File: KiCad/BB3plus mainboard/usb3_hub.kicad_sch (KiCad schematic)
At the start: 73 parts, among them IC16 USB5807C/KD, IC17 TPS62933ODRLR, Y2 VXM7-9032-25M0000000

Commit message: #23
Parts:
- R62, R63: now fitted; now in the parts list
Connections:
- net HUB_VBUS_EN: no longer names the net of IC16.24 (VBUS_DET), R62.2, R63.2
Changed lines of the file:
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@@
 	(title_block
 		(title "${project_name}")
-		(date "2026-10-08")
+		(date "2026-10-09")
 		(rev "${project_version}")
 		(company "${project_creator}")
@@
 	)
 	(junction
-		(at 58.42 22.86)
-		(diameter 0)
-		(color 0 0 0 0)
-	)
-	(junction
 		(at 43.18 55.88)
 		(diameter 0)
@@
 		)
 	)
-	(wire
-		(pts
-			(xy 48.26 17.78) (xy 58.42 17.78)
-		)
-		(stroke
-			(width 0)
-			(type default)
-		)
-	)
 	(polyline
 		(pts
@@
 		)
 	)
-	(wire
-		(pts
-			(xy 58.42 17.78) (xy 58.42 22.86)
-		)
-		(stroke
-			(width 0)
-			(type default)
-		)
-	)
 	(polyline
 		(pts
@@
 		)
 	)
-	(global_label "HUB_VBUS_EN"
-		(shape input)
-		(at 48.26 17.78 180)
-		(fields_autoplaced yes)
-		(effects
-			(font
-				(size 0.889 0.889)
-				(color 204 102 0 1)
-			)
-			(justify right)
-		)
-		(property "Intersheetrefs" "${INTERSHEET_REFS}"
-			(at 37.3576 17.78 0)
-			(hide yes)
-			(show_name no)
-			(do_not_autoplace no)
-			(effects
-				(font
-					(size 1.27 1.27)
-				)
-				(justify right)
-			)
-		)
-	)
 	(global_label "DIB4_USB_RX+"
 		(shape input)
@@
 		(body_style 1)
 		(exclude_from_sim no)
-		(in_bom no)
+		(in_bom yes)
 		(on_board yes)
-		(in_pos_files no)
-		(dnp yes)
+		(in_pos_files yes)
+		(dnp no)
 		(property "Reference" "R62"
 			(at 50.8 21.59 90)
@@
 		(body_style 1)
 		(exclude_from_sim no)
-		(in_bom no)
+		(in_bom yes)
 		(on_board yes)
-		(in_pos_files no)
-		(dnp yes)
+		(in_pos_files yes)
+		(dnp no)
 		(property "Reference" "R63"
 			(at 50.8 29.21 90)

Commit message: PE fault detection section updated
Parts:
- renumbered C99 to C100, C100 to C101, C101 to C102, C102 to C103, C103 to C104, C104 to C105, C105 to C106, C106 to C107, C107 to C108, C108 to C109, C109 to C110, C110 to C111, C67 to C68, C68 to C69, C69 to C70, C70 to C71, C71 to C72, C72 to C73, C73 to C74, C74 to C75, C75 to C76, C76 to C77, C77 to C78, C78 to C79, C79 to C80, C80 to C81, C81 to C82, C82 to C83, C83 to C84, C84 to C85, C85 to C86, C86 to C87, C87 to C88, C88 to C89, C89 to C90, C90 to C91, C91 to C92, C92 to C93, C93 to C94, C94 to C95, C95 to C96, C96 to C97, C97 to C98, C98 to C99, JP10 to JP12, JP11 to JP13, JP12 to JP14, JP13 to JP15

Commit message: #24
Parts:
- renumbered C102 to C100, C103 to C101, C104 to C102, C105 to C103, C106 to C104, C107 to C105, C108 to C106, C109 to C107, C110 to C108, C111 to C109, C68 to C66, C69 to C67, C70 to C68, C71 to C69, C72 to C70, C73 to C71, C74 to C72, C75 to C73, C76 to C74, C77 to C75, C78 to C76, C79 to C77, C80 to C78, C81 to C79, C82 to C80, C83 to C81, C84 to C82, C85 to C83, C86 to C84, C87 to C85, C88 to C86, C89 to C87, C90 to C88, C91 to C89, C92 to C90, C93 to C91, C94 to C92, C95 to C93, C96 to C94, C97 to C95, C98 to C96, C99 to C97, C100 to C98, C101 to C99, IC16 to IC13, IC17 to IC14, JP12 to JP11, JP13 to JP12, JP14 to JP13, JP15 to JP14, R60 to R57, R61 to R58, R62 to R59, R63 to R60, R64 to R61, R65 to R62, R66 to R63, R67 to R64, R68 to R65, R69 to R66, R70 to R67, R71 to R68, R72 to R69, R73 to R70, R74 to R71, R75 to R72, R76 to R73, R77 to R74

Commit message: USB CC wiring updated
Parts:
- R63: value 200K -> 10K; DigiKey 13-RC0603FR-13200KLCT-ND -> 1712-CRGH0603F10KCT-ND; LCSC C25811 -> C25804; Mouser 603-RC0603FR-13200KL -> 756-WCR0603-10KFI; TME SMD0603-200K-1% -> SMD0603-10K-1%
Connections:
- net +3V3: no longer R63.1
- net GND: now also R63.1
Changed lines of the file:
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@@
 	(title_block
 		(title "${project_name}")
-		(date "2026-10-12")
+		(date "2026-10-14")
 		(rev "${project_version}")
 		(company "${project_creator}")
@@
 		)
 	)
-	(text_box "Battery charging enabled on P1 "
+	(text_box "Battery charging enabled on P1, P2"
 		(exclude_from_sim no)
-		(at 20.955 54.61 0)
-		(size 12.7 3.81)
+		(at 19.05 57.785 0)
+		(size 14.605 4.195)
 		(margins 0.6668 0.6668 0.6668 0.6668)
 		(stroke
@@
 	)
 	(junction
-		(at 43.18 55.88)
+		(at 43.18 58.42)
 		(diameter 0)
 		(color 0 0 0 0)
@@
 		)
 	)
+	(wire
+		(pts
+			(xy 43.18 58.42) (xy 43.18 60.96)
+		)
+		(stroke
+			(width 0)
+			(type default)
+		)
+	)
 	(polyline
 		(pts
@@
 	(wire
 		(pts
-			(xy 33.02 60.96) (xy 45.72 60.96)
-		)
-		(stroke
-			(width 0)
-			(type default)
-		)
-	)
-	(wire
-		(pts
 			(xy 53.34 142.24) (xy 58.42 142.24)
 		)
@@
 	(wire
 		(pts
+			(xy 43.18 60.96) (xy 45.72 60.96)
+		)
+		(stroke
+			(width 0)
+			(type default)
+		)
+	)
+	(wire
+		(pts
 			(xy 40.64 147.32) (xy 40.64 152.4)
 		)
@@
 	(wire
 		(pts
+			(xy 43.18 58.42) (xy 43.18 55.88)
+		)
+		(stroke
+			(width 0)
+			(type default)
+		)
+	)
+	(wire
+		(pts
 			(xy 271.78 147.32) (xy 274.32 147.32)
 		)
@@
 	(wire
 		(pts
-			(xy 43.18 55.88) (xy 43.18 58.42)
-		)
-		(stroke
-			(width 0)
-			(type default)
-		)
-	)
-	(wire
-		(pts
 			(xy 116.84 167.64) (xy 134.62 167.64)
 		)
@@
 	(wire
 		(pts
-			(xy 40.64 55.88) (xy 43.18 55.88)
+			(xy 40.64 58.42) (xy 43.18 58.42)
 		)
 		(stroke
@@
 		(in_pos_files yes)
 		(dnp no)
-		(property "Reference" "#+3V029"
+		(property "Reference" "#+3V028"
 			(at 279.4 30.48 0)
 			(hide yes)
@@
 			(project "BB3plus mainboard"
 				(path "/1df84e4f-233a-4f72-9418-c0020706bb76/99b67fa5-56ce-4798-a21a-d86c3d347c55"
-					(reference "#+3V029")
-					(unit 1)
-				)
-			)
-		)
-	)
-	(symbol
-		(lib_id "PCM_EEZ_symbols:+3V3")
-		(at 30.48 60.96 90)
-		(mirror x)
-		(unit 1)
-		(body_style 1)
-		(exclude_from_sim no)
-		(in_bom yes)
-		(on_board yes)
-		(in_pos_files yes)
-		(dnp no)
-		(property "Reference" "#+3V027"
-			(at 30.48 60.96 0)
-			(hide yes)
-			(show_name no)
-			(do_not_autoplace no)
-			(effects
-				(font
-					(size 1.27 1.27)
-				)
-			)
-		)
-		(property "Value" "+3V3"
-			(at 24.765 61.595 90)
-			(show_name no)
-			(do_not_autoplace no)
-			(effects
-				(font
-					(size 1.27 1.27)
-				)
-				(justify right bottom)
-			)
-		)
-		(property "Footprint" ""
-			(at 30.48 60.96 0)
-			(hide yes)
-			(show_name no)
-			(do_not_autoplace no)
-			(effects
-				(font
-					(size 1.27 1.27)
-				)
-			)
-		)
-		(property "Datasheet" ""
-			(at 30.48 60.96 0)
-			(hide yes)
-			(show_name no)
-			(do_not_autoplace no)
-			(effects
-				(font
-					(size 1.27 1.27)
-				)
-			)
-		)
-		(property "Description" ""
-			(at 30.48 60.96 0)
-			(hide yes)
-			(show_name no)
-			(do_not_autoplace no)
-			(effects
-				(font
-					(size 1.27 1.27)
-				)
-			)
-		)
-		(pin "1"
-		)
-		(instances
-			(project "BB3plus mainboard"
-				(path "/1df84e4f-233a-4f72-9418-c0020706bb76/99b67fa5-56ce-4798-a21a-d86c3d347c55"
-					(reference "#+3V027")
+					(reference "#+3V028")
 					(unit 1)
 				)
@@
 	(symbol
 		(lib_id "power:GND")
-		(at 40.64 55.88 0)
+		(at 40.64 58.42 0)
 		(mirror y)
 		(unit 1)
@@
 		(dnp no)
 		(property "Reference" "#PWR021"
-			(at 40.64 62.23 0)
+			(at 40.64 64.77 0)
 			(hide yes)
 			(show_name no)
@@
 		)
 		(property "Value" "GND"
-			(at 39.37 57.785 0)
+			(at 39.37 60.325 0)
 			(show_name no)
 			(do_not_autoplace no)
@@
 		)
 		(property "Footprint" ""
-			(at 40.64 55.88 0)
+			(at 40.64 58.42 0)
 			(hide yes)
 			(show_name no)
@@
 		)
 		(property "Datasheet" ""
-			(at 40.64 55.88 0)
+			(at 40.64 58.42 0)
 			(hide yes)
 			(show_name no)
@@
 		)
 		(property "Description" "Power symbol creates a global label with name \"GND\" , ground"
-			(at 40.64 55.88 0)
+			(at 40.64 58.42 0)
 			(hide yes)
 			(show_name no)
@@
 			)
 		)
-		(property "Value" "200K"
+		(property "Value" "10K"
 			(at 53.975 60.96 90)
 			(show_name no)
@@
 			)
 		)
-		(property "DigiKey" "13-RC0603FR-13200KLCT-ND"
+		(property "DigiKey" "1712-CRGH0603F10KCT-ND"
 			(at 50.8 60.96 0)
 			(hide yes)
@@
 			)
 		)
-		(property "Mouser" "603-RC0603FR-13200KL "
+		(property "Mouser" "756-WCR0603-10KFI"
 			(at 50.8 60.96 0)
 			(hide yes)
@@
 			)
 		)
-		(property "TME" "SMD0603-200K-1%"
+		(property "TME" "SMD0603-10K-1%"
 			(at 50.8 60.96 0)
 			(hide yes)
@@
 			)
 		)
-		(property "LCSC" "C25811"
+		(property "LCSC" "C25804"
 			(at 50.8 60.96 0)
 			(hide yes)
@@
 		(in_pos_files yes)
 		(dnp no)
-		(property "Reference" "#+3V028"
+		(property "Reference" "#+3V027"
 			(at 38.1 71.12 0)
 			(hide yes)
@@
 			(project "BB3plus mainboard"
 				(path "/1df84e4f-233a-4f72-9418-c0020706bb76/99b67fa5-56ce-4798-a21a-d86c3d347c55"
-					(reference "#+3V028")
+					(reference "#+3V027")
 					(unit 1)
 				)

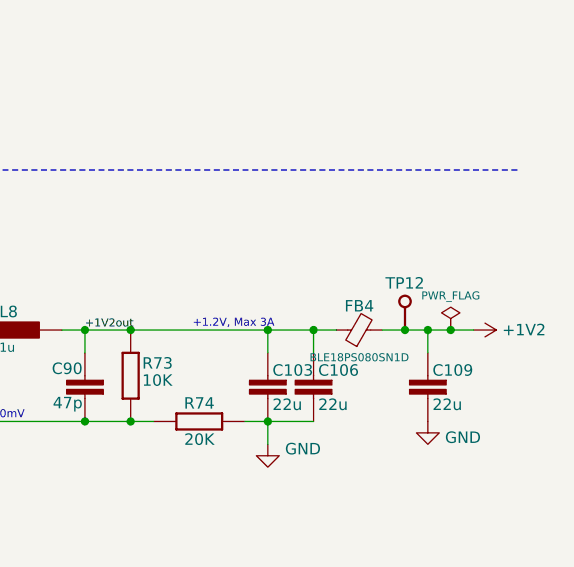
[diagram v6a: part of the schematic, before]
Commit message: Rear USB & Ethernet updated
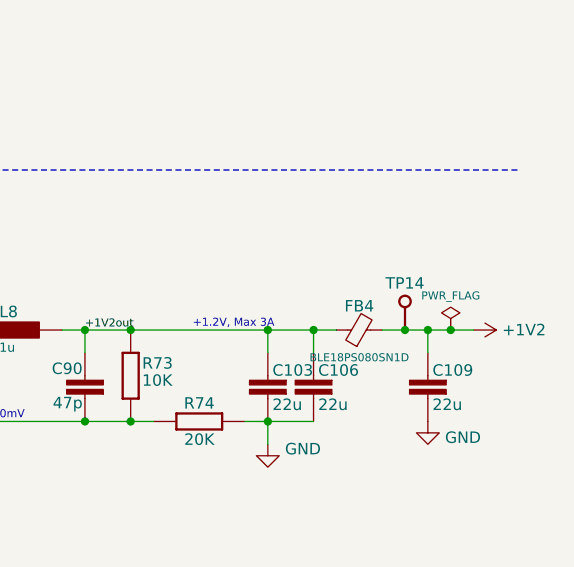
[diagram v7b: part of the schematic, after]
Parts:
- renumbered TP12 to TP14
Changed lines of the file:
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@@
 		(in_bom no)
 		(on_board yes)
-		(in_pos_files yes)
+		(in_pos_files no)
 		(dnp no)
 		(property "Reference" "JP13"
@@
 		(in_pos_files yes)
 		(dnp no)
-		(property "Reference" "TP12"
+		(property "Reference" "TP14"
 			(at 269.24 142.875 90)
 			(show_name no)
@@
 			(project "BB3plus mainboard"
 				(path "/1df84e4f-233a-4f72-9418-c0020706bb76/99b67fa5-56ce-4798-a21a-d86c3d347c55"
-					(reference "TP12")
+					(reference "TP14")
 					(unit 1)
 				)
@@
 		(in_bom no)
 		(on_board yes)
-		(in_pos_files yes)
+		(in_pos_files no)
 		(dnp no)
 		(property "Reference" "JP14"
@@
 		(in_bom no)
 		(on_board yes)
-		(in_pos_files yes)
+		(in_pos_files no)
 		(dnp no)
 		(property "Reference" "JP12"
